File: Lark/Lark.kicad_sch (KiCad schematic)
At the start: 0 parts

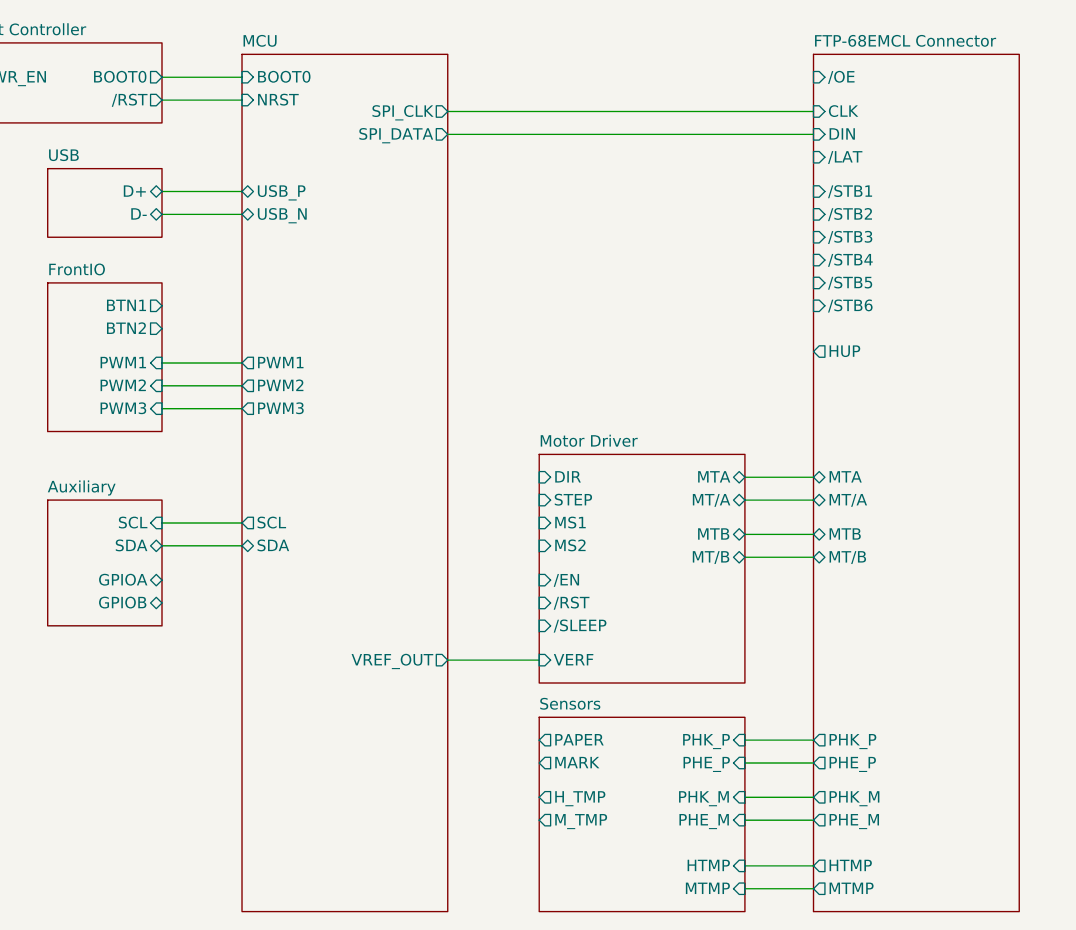
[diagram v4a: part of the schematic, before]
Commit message: Updated schematic, WIP
- Added NOR flash part.
- Added new CubeMX config file.
- Reannotated the schematic.
- Made some more connections to the MCU.
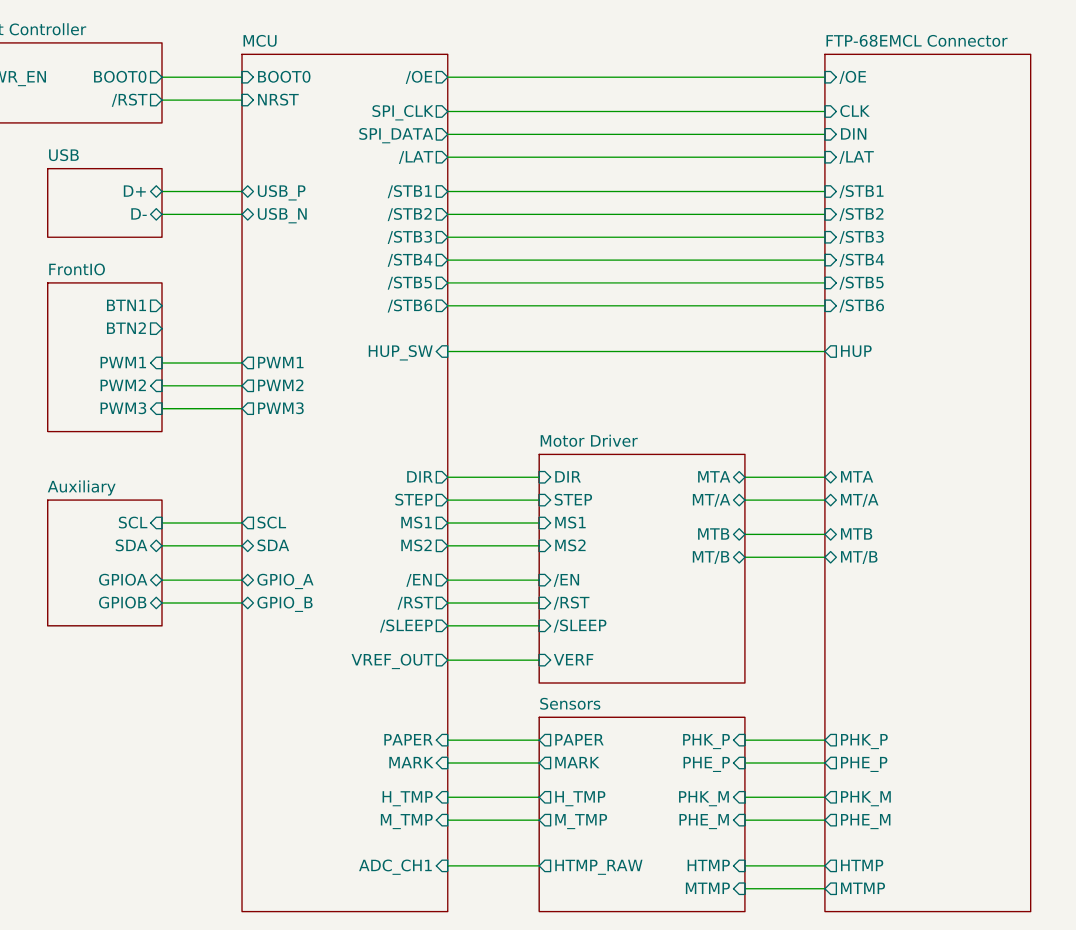
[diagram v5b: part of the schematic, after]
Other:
- sheet MCU ports: added ADC_CH1, DIR, GPIO_A, GPIO_B, HUP_SW, H_TMP, MARK, MS1, MS2, M_TMP, PAPER, STEP, /EN, /LAT, /OE, /RST, /SLEEP, /STB1, /STB2, /STB3, /STB4, /STB5, /STB6; removed none
- sheet Sensors ports: added HTMP_RAW; removed none

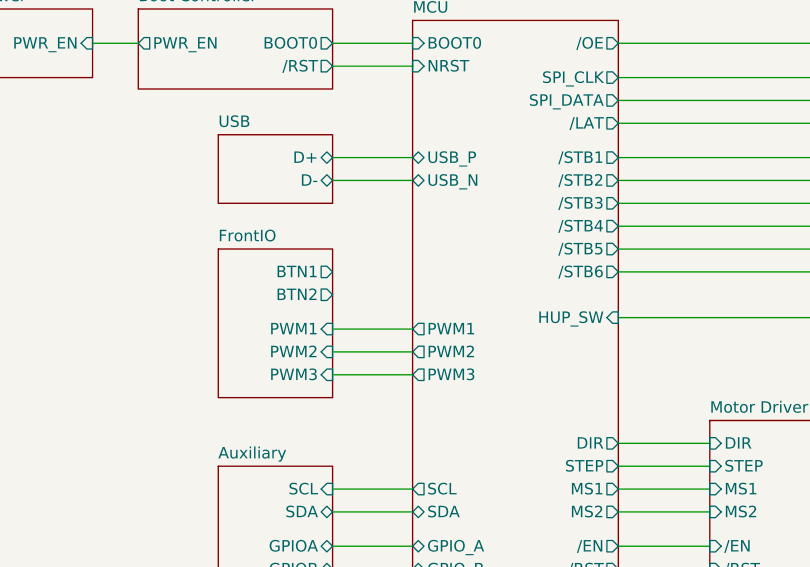
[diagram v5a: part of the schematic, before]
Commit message: The right side of the board is finalized.
- Finalized the logic side of the board (right)
- Will work on the power section next.
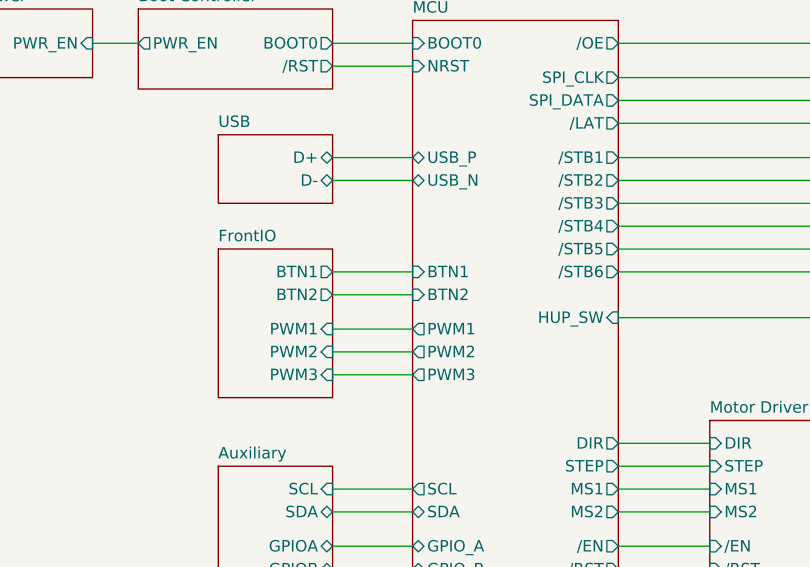
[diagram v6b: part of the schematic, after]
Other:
- sheet MCU ports: added BTN1, BTN2; removed none
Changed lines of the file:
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@@
+	(wire
+		(pts
+			(xy 96.52 73.66) (xy 105.41 73.66)
+		)
+		(stroke
+			(width 0)
+			(type default)
+		)
+	)
 	(wire
 		(pts
@@
 		(pts
 			(xy 128.27 71.12) (xy 170.18 71.12)
+		)
+		(stroke
+			(width 0)
+			(type default)
+		)
+	)
+	(wire
+		(pts
+			(xy 96.52 76.2) (xy 105.41 76.2)
 		)
 		(stroke
@@
 			)
 		)
+		(pin "BTN1" input
+			(at 105.41 73.66 180)
+			(effects
+				(font
+					(size 1.27 1.27)
+				)
+				(justify left)
+			)
+		)
+		(pin "BTN2" input
+			(at 105.41 76.2 180)
+			(effects
+				(font
+					(size 1.27 1.27)
+				)
+				(justify left)
+			)
+		)

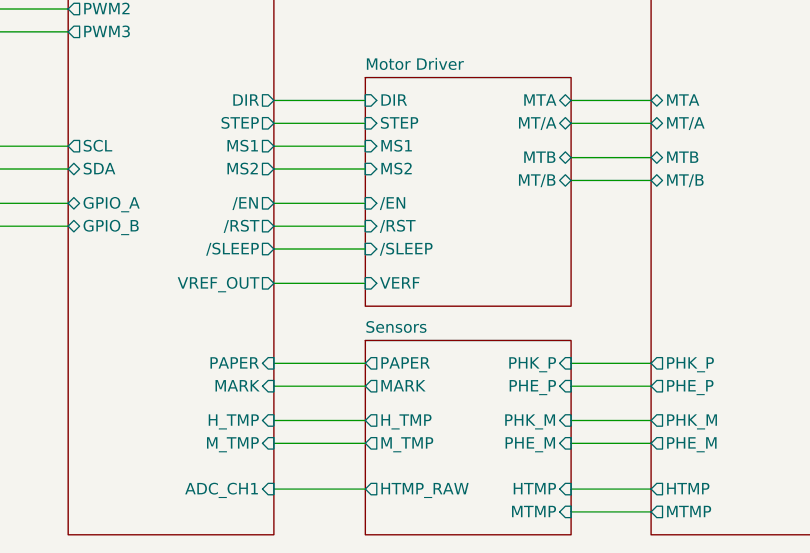
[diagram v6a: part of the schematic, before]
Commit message: minor updates
- changed npn pins to passive.
- changed rev to match working revision.
- minor PCB changes.
- moved TVS diode next to connector.
- changed barrel jack silkscreen.
- changed usbc silkscreen.
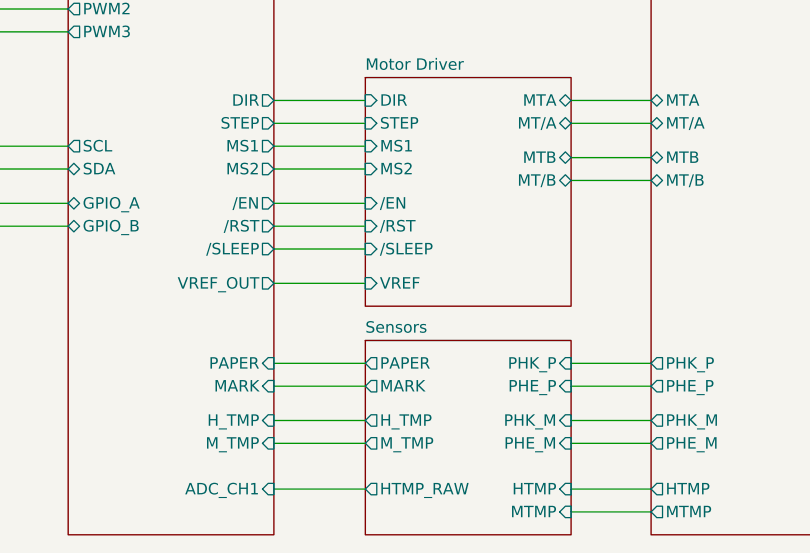
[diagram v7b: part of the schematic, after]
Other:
- sheet Motor Driver ports: added VREF; removed VERF
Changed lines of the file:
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@@
 		(title "Lark Print Engine")
 		(date "2025-10-08")
-		(rev "01.00.01")
+		(rev "01.00.00")
 		(comment 1 "Thermal Print Engine")
 		(comment 2 "Designer: HamSlices")
@@
 			)
 		)
-		(pin "VERF" input
+		(pin "VREF" input
 			(at 138.43 113.03 180)
 			(effects
